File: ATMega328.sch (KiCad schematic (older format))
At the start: 8 parts, among them J2 AVR-ISP-6, U1 ATmega328P-AU, Y1 Crystal_GND24

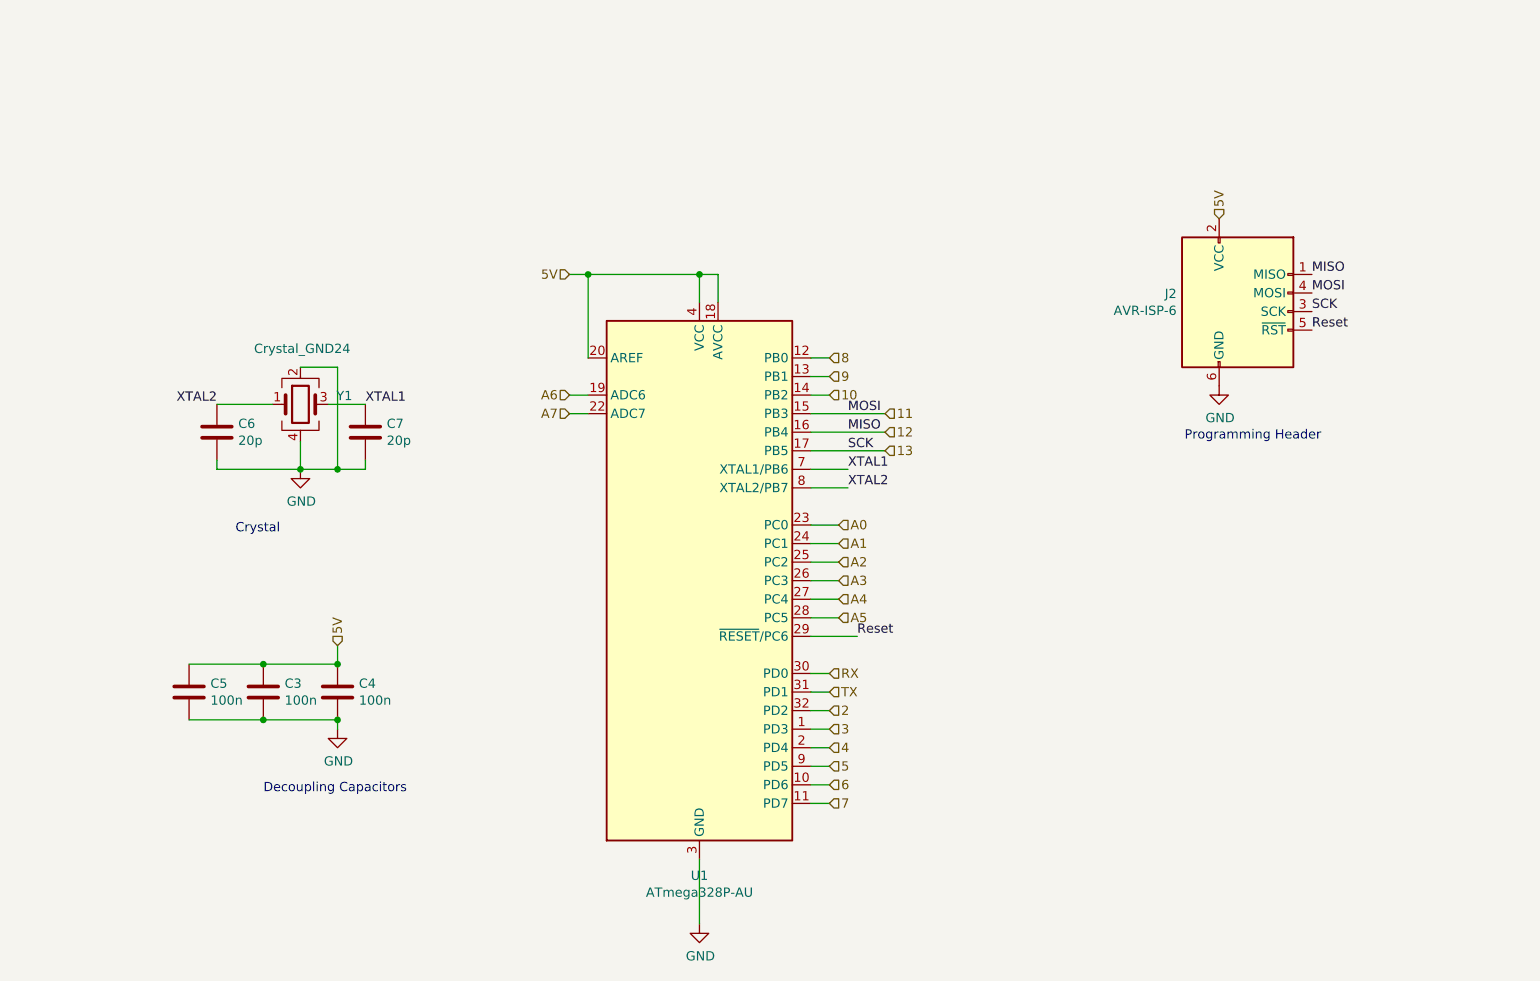
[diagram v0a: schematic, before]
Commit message: Version 2 PCB fully routed, simulations added
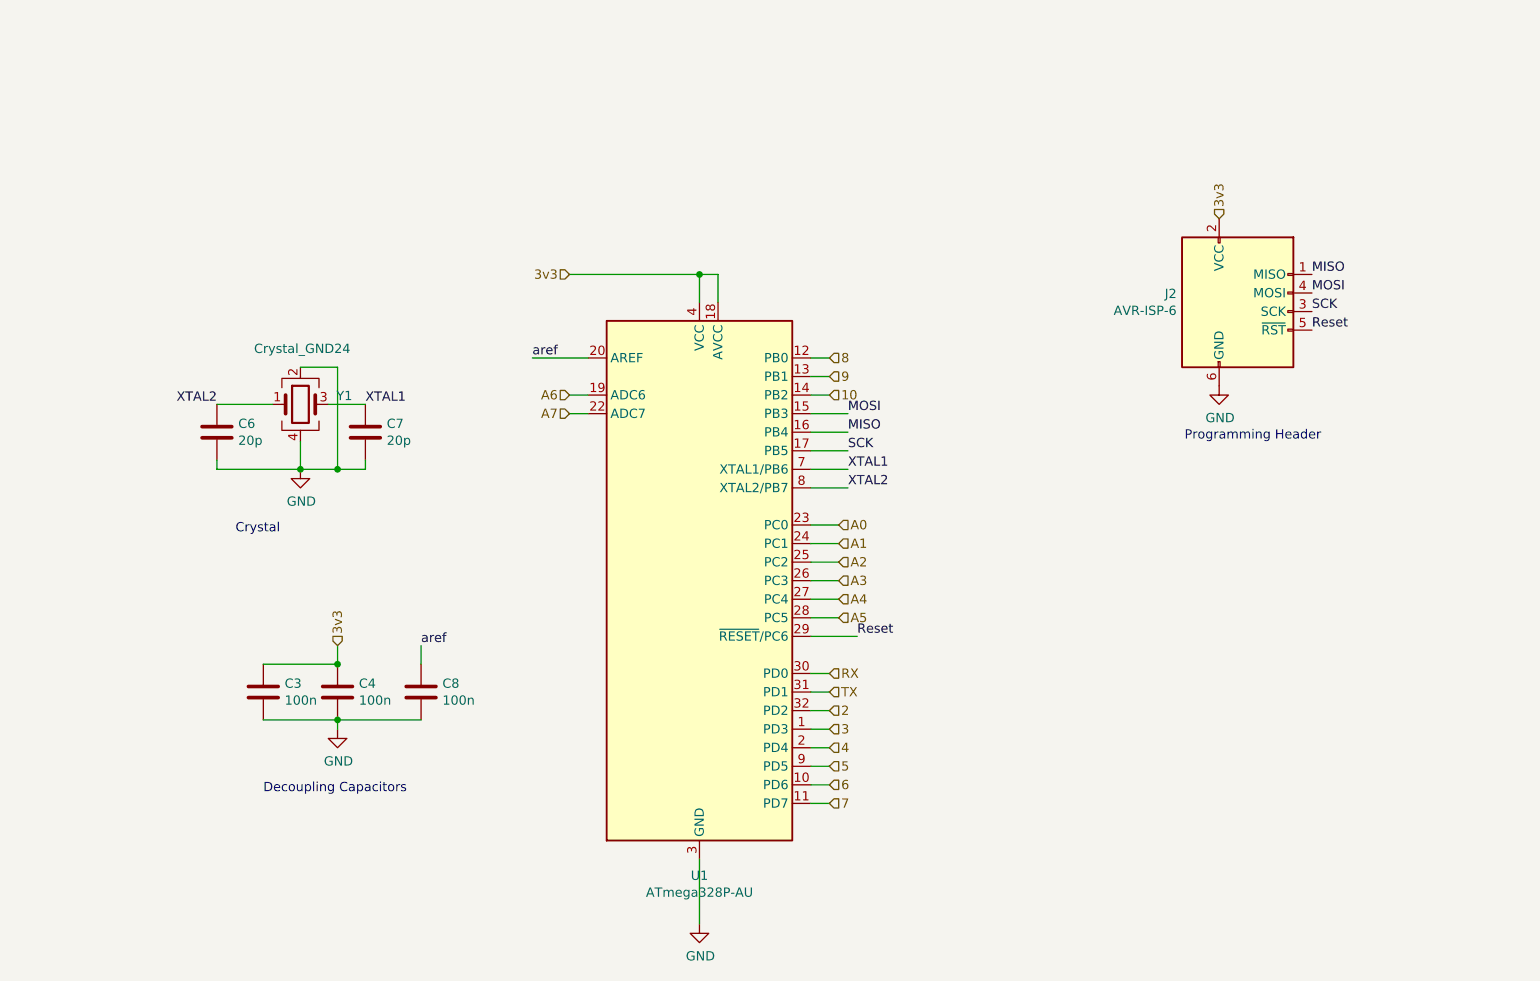
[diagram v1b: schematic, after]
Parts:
- removed C5: 100n, Capacitor_SMD:C_0201_0603Metric, symbol Device:C
- added C8: 100n, Capacitor_SMD:C_0201_0603Metric, symbol Device:C
- J2: footprint (none) -> Connector_PinHeader_2.54mm:PinHeader_2x03_P2.54mm_Vertical
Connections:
- net GND: now also C8.2
- net 11 renamed MOSI
- net 12 renamed MISO
- net 13 renamed SCK
- net 5V renamed 3v3
- net 3v3: no longer U1.20 (AREF)
- new net aref: C8.1, U1.20 (AREF)
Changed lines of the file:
@@
 $EndComp
 Text HLabel 5100 2250 0    50   Input ~ 0
-5V
+3v3
 $Comp
 L power:GND #PWR0109
@@
 	5800 5750 5800 5400
 Wire Wire Line
-	5100 2250 5200 2250
-Wire Wire Line
 	5900 2400 5900 2250
 Wire Wire Line
@@
 Wire Wire Line
 	5800 2250 5900 2250
-Wire Wire Line
-	5200 2700 5200 2250
-Connection ~ 5200 2250
-Wire Wire Line
-	5200 2250 5800 2250
 $Comp
 L Device:C C3
@@
 	3850 4650 3450 4650
 Text HLabel 3850 4250 1    50   Input ~ 0
-5V
+3v3
 Wire Wire Line
 	3850 4250 3850 4350
@@
 MOSI
 Text HLabel 8600 1950 1    50   Input ~ 0
-5V
+3v3
 $Comp
 L power:GND #PWR0113
@@
 Wire Wire Line
 	6400 2900 6500 2900
-Text HLabel 6800 3000 2    50   Input ~ 0
-11
-Text HLabel 6800 3100 2    50   Input ~ 0
-12
-Text HLabel 6800 3200 2    50   Input ~ 0
-13
-Wire Wire Line
-	6400 3000 6800 3000
-Wire Wire Line
-	6400 3100 6800 3100
-Wire Wire Line
-	6400 3200 6800 3200
 Text HLabel 5100 2900 0    50   Input ~ 0
 A6
@@
 F 0 "J2" H 8371 2546 50  0000 R CNN
 F 1 "AVR-ISP-6" H 8371 2455 50  0000 R CNN
-F 2 "" V 8450 2500 50  0001 C CNN
+F 2 "Connector_PinHeader_2.54mm:PinHeader_2x03_P2.54mm_Vertical" V 8450 2500 50  0001 C CNN
 F 3 " ~" H 7425 1900 50  0001 C CNN
 	1    8700 2450
@@
 $EndComp
 $Comp
-L Device:C C5
-U 1 1 60E73517
-P 3050 4500
-F 0 "C5" H 3165 4546 50  0000 L CNN
-F 1 "100n" H 3165 4455 50  0000 L CNN
-F 2 "Capacitor_SMD:C_0201_0603Metric" H 3088 4350 50  0001 C CNN
-F 3 "~" H 3050 4500 50  0001 C CNN
-	1    3050 4500
-	1    0    0    -1
-$EndComp
-$Comp
 L Device:C C6
 U 1 1 60E74F12
@@
 $EndComp
 Wire Wire Line
-	3050 4350 3450 4350
-Connection ~ 3450 4350
-Wire Wire Line
-	3050 4650 3450 4650
-Connection ~ 3450 4650
-Wire Wire Line
 	3200 2950 3500 2950
 Wire Wire Line
@@
 Wire Wire Line
 	3850 3300 4000 3300
+$Comp
+L Device:C C8
+U 1 1 618F06A7
+P 4300 4500
+F 0 "C8" H 4415 4546 50  0000 L CNN
+F 1 "100n" H 4415 4455 50  0000 L CNN
+F 2 "Capacitor_SMD:C_0201_0603Metric" H 4338 4350 50  0001 C CNN
+F 3 "~" H 4300 4500 50  0001 C CNN
+	1    4300 4500
+	1    0    0    -1
+$EndComp
+Wire Wire Line
+	4300 4650 3850 4650
+Wire Wire Line
+	4300 4350 4300 4250
+Text Label 4300 4250 0    50   ~ 0
+aref
+Wire Wire Line
+	5100 2250 5800 2250
+Wire Wire Line
+	5200 2700 4900 2700
+Text Label 4900 2700 0    50   ~ 0
+aref
+Wire Wire Line
+	6400 3000 6600 3000
+Wire Wire Line
+	6400 3100 6600 3100
+Wire Wire Line
+	6400 3200 6600 3200
 $EndSCHEMATC

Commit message: Version 0.3 prototype - Manufactured
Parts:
- C3, C4, C6, C7, C8: footprint Capacitor_SMD:C_0201_0603Metric -> Capacitor_SMD:C_0603_1608Metric
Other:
- moved on the sheet: C3, C4, C6, C7, C8, J2, U1, Y1
